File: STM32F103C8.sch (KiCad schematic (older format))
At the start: 0 parts

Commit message: STM32F103C8
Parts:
- added U?: STM32F103C8Tx, Package_QFP:LQFP-48_7x7mm_P0.5mm, symbol MCU_ST_STM32F1:STM32F103C8Tx
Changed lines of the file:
@@
 $Descr A4 11693 8268
 encoding utf-8
-Sheet 1 1
+Sheet 5 5
 Title ""
 Date ""
@@
 Comment4 ""
 $EndDescr
+$Comp
+L MCU_ST_STM32F1:STM32F103C8Tx U?
+U 1 1 5CEC658E
+P 5600 3900
+F 0 "U?" H 5550 2311 50  0000 C CNN
+F 1 "STM32F103C8Tx" H 5550 2220 50  0000 C CNN
+F 2 "Package_QFP:LQFP-48_7x7mm_P0.5mm" H 5000 2500 50  0001 R CNN
+F 3 "http://www.st.com/st-web-ui/static/active/en/resource/technical/document/datasheet/CD00161566.pdf" H 5600 3900 50  0001 C CNN
+	1    5600 3900
+	1    0    0    -1
+$EndComp
 $EndSCHEMATC

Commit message: USB - Boot sel - Serial - STM32
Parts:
- added C? (x2): 20p, Capacitor_SMD:C_0805_2012Metric_Pad1.15x1.40mm_HandSolder, symbol Device:C
- added C? (x4): 100n, Capacitor_SMD:C_0805_2012Metric_Pad1.15x1.40mm_HandSolder, symbol Device:C
- added D?: LED, LED_SMD:LED_0805_2012Metric_Pad1.15x1.40mm_HandSolder, symbol Device:LED
- added J?: UART, Connector_PinHeader_2.54mm:PinHeader_1x04_P2.54mm_Vertical, symbol Connector_Generic:Conn_01x04
- added J?: BOOT, Connector_PinHeader_2.54mm:PinHeader_2x03_P2.54mm_Vertical, symbol Connector_Generic:Conn_02x03_Odd_Even
- added J?: USB_B_Micro, symbol Connector:USB_B_Micro
- added R?: 1k, Resistor_SMD:R_0805_2012Metric_Pad1.15x1.40mm_HandSolder, symbol Device:R
- added R?: 0R, Resistor_SMD:R_0805_2012Metric_Pad1.15x1.40mm_HandSolder, symbol Device:R
- added R?: 0R, Jumper:SolderJumper-2_P1.3mm_Bridged_RoundedPad1.0x1.5mm, symbol Device:R
- added R? (x2): 100k, Resistor_SMD:R_0805_2012Metric_Pad1.15x1.40mm_HandSolder, symbol Device:R
- added R? (x2): 10k, Resistor_SMD:R_0805_2012Metric_Pad1.15x1.40mm_HandSolder, symbol Device:R
- added R?: 1k5, Resistor_SMD:R_0805_2012Metric_Pad1.15x1.40mm_HandSolder, symbol Device:R
- added R?: 10R, Resistor_SMD:R_0805_2012Metric_Pad1.15x1.40mm_HandSolder, symbol Device:R
- added U?: AMS1117-3.3, Package_TO_SOT_SMD:SOT-223-3_TabPin2, symbol Regulator_Linear:AMS1117-3.3
- added Y?: 8 MHz, Crystal:Crystal_HC49-U_Vertical, symbol Device:Crystal
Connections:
- net STM32_PA0: now reaches U?.10 (PA0)
- net STM32_PA1: now reaches U?.11 (PA1)
- net STM32_PA2: now reaches U?.12 (PA2)
- net STM32_PA3: now reaches U?.13 (PA3)
- net STM32_PA4: now reaches U?.14 (PA4)
- net STM32_PA5: now reaches U?.15 (PA5)
- net STM32_PA6: now reaches U?.16 (PA6)
- net STM32_PA7: now reaches U?.17 (PA7)
- net STM32_PB0: now reaches U?.18 (PB0)
- net STM32_PB1: now reaches U?.19 (PB1)
- net STM32_PC13: now reaches U?.2 (PC13)
- net STM32_PB2: now reaches U?.20 (PB2)
- net STM32_PB2: now also R?.2
- net STM32_PB10: now reaches U?.21 (PB10)
- net STM32_PB11: now reaches U?.22 (PB11)
- net GND: now reaches U?.23 (VSS)
- net GND: now also U?.35 (VSS), U?.47 (VSS), C?.1, C?.1, C?.1, C?.2, C?.2, D?.1 (K), J?.1 (Pin_1), J?.2 (Pin_2), J?.4 (Pin_4), J?.5 (GND), J?.6 (Shield), R?.2, U?.1 (GND)
- net +3V3: now reaches U?.24 (VDD)
- net +3V3: now also U?.36 (VDD), U?.48 (VDD), C?.2, C?.2, C?.2, J?.1 (Pin_1), J?.5 (Pin_5), J?.6 (Pin_6), R?.1, R?.2, R?.2, R?.2, U?.2 (VO)
- net STM32_PB12: now reaches U?.25 (PB12)
- net STM32_PB13: now reaches U?.26 (PB13)
- net STM32_PB14: now reaches U?.27 (PB14)
- net STM32_PB15: now reaches U?.28 (PB15)
- net STM32_PA8: now reaches U?.29 (PA8)
- net STM32_PC14: now reaches U?.3 (PC14)
- net STM32_PA9: now reaches U?.30 (PA9)
- net STM32_PA10: now reaches U?.31 (PA10)
- net STM32_PA11: now reaches U?.32 (PA11)
- net STM32_PA11: now also J?.2 (D-)
- net STM32_PA12: now reaches U?.33 (PA12)
- net STM32_PA12: now also J?.3 (D+), R?.2
- net STM32_PA13: now reaches U?.34 (PA13)
- net STM32_PA13: now also J?.2 (Pin_2), R?.1
- net STM32_PA14: now reaches U?.37 (PA14)
- net STM32_PA14: now also J?.3 (Pin_3), R?.1
- net STM32_PA15: now reaches U?.38 (PA15)
- net STM32_PB3: now reaches U?.39 (PB3)
- net STM32_PC15: now reaches U?.4 (PC15)
- net STM32_PB4: now reaches U?.40 (PB4)
- net STM32_PB5: now reaches U?.41 (PB5)
- net STM32_PB6: now reaches U?.42 (PB6)
- net STM32_PB7: now reaches U?.43 (PB7)
- net STM32_Boot0: now reaches U?.44 (BOOT0)
- net STM32_Boot0: now also R?.2
- net STM32_PB8: now reaches U?.45 (PB8)
- net STM32_PB9: now reaches U?.46 (PB9)
- net at U?.5 (PD0): now also C?.1, Y?.1
- net at U?.6 (PD1): now also C?.1, Y?.2
- net STM32_reset: now reaches U?.7 (NRST)
- net GNDA: now reaches U?.8 (VSSA)
- net GNDA: now also C?.1, R?.1
- net +3.3VA: now reaches U?.9 (VDDA)
- net +3.3VA: now also C?.2, R?.1
- new net: D?.2 (A), R?.1
- new net: J?.3 (Pin_3), R?.1
- new net: J?.4 (Pin_4), R?.1
- new net: J?.1 (VBUS), R?.1
- new net +5V: R?.2, U?.3 (VI)
- new net 0_LED: R?.2
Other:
- note added: "Annotation according to \nhttps://github.com/MCUdude/MightyCore"

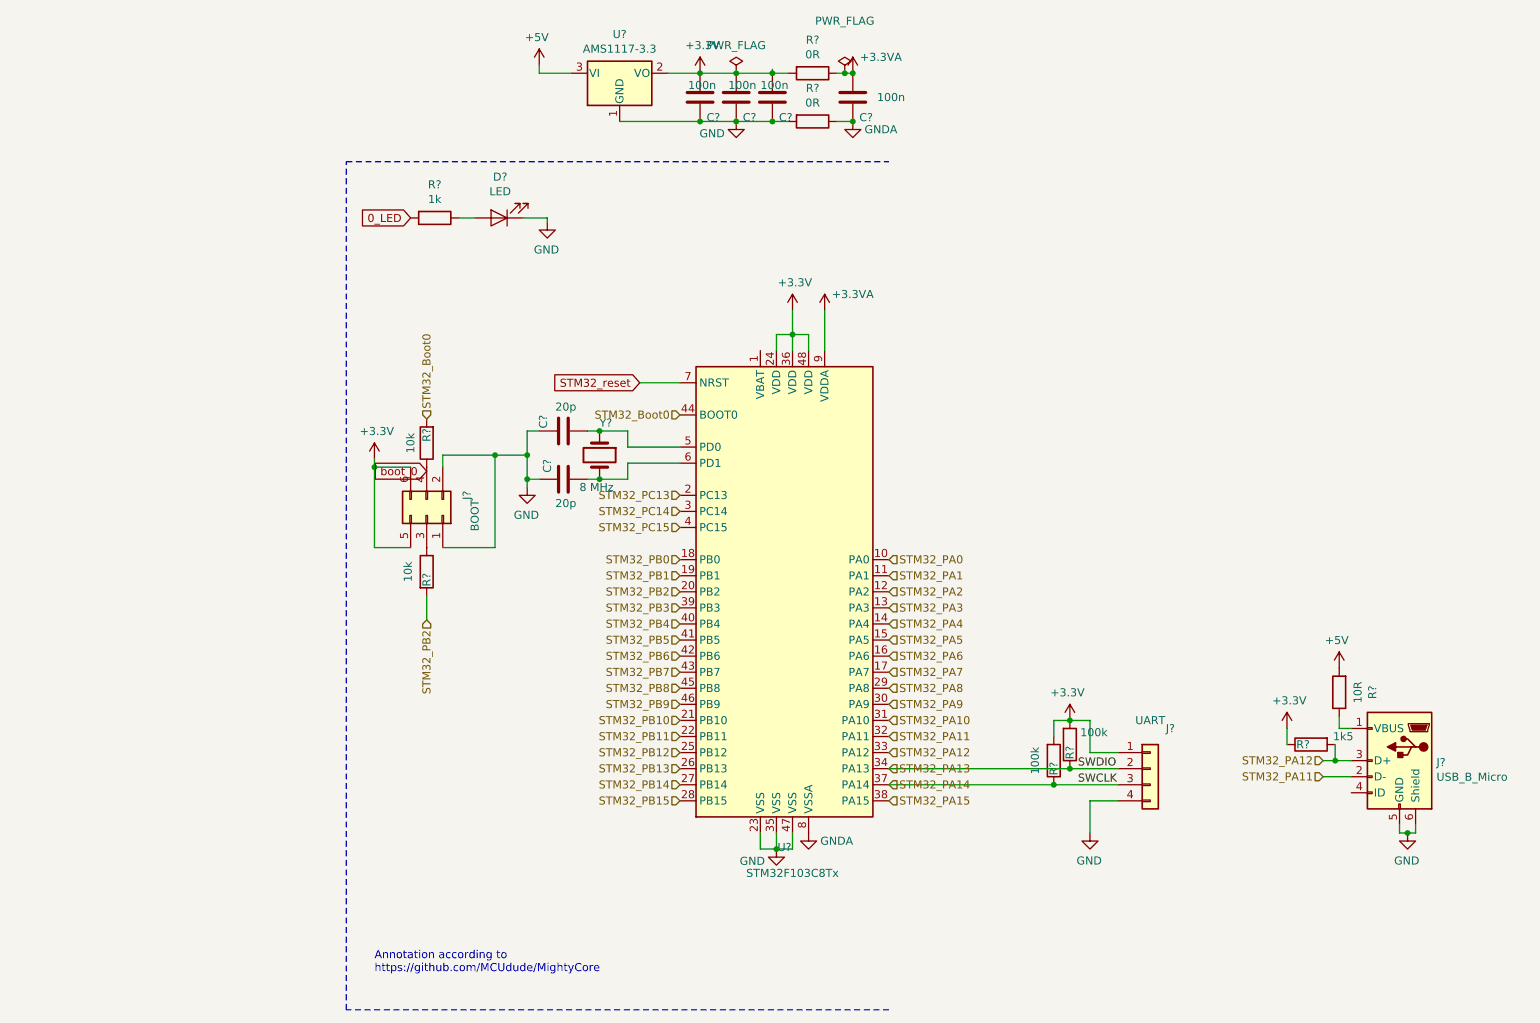
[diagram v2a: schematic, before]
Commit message: STM32 DAC and Analog input
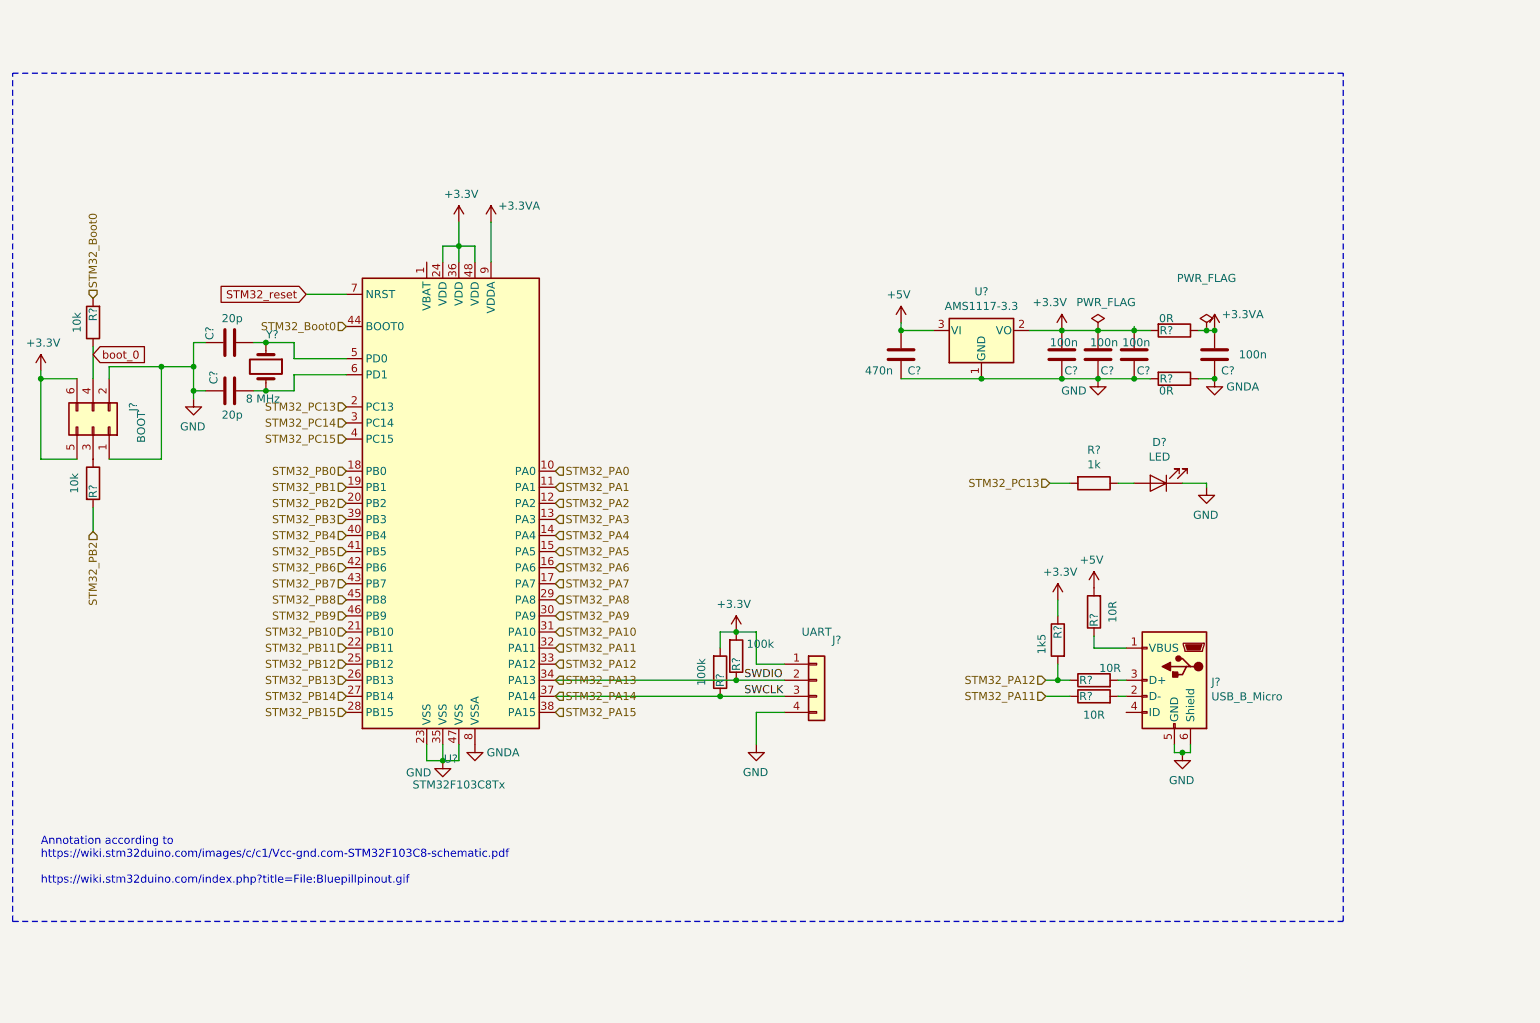
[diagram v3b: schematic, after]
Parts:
- added C?: 470n, Capacitor_SMD:C_0805_2012Metric_Pad1.15x1.40mm_HandSolder, symbol Device:C
- added R? (x2): 10R, Resistor_SMD:R_0805_2012Metric_Pad1.15x1.40mm_HandSolder, symbol Device:R
- J?: footprint (none) -> Connector_USB:USB_Micro-B_Wuerth_629105150521
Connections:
- net 0_LED is gone; now on net STM32_PC13: R?.2
- net +5V: now also C?.2
- net GND: now also C?.1
- net STM32_PA11: now also R?.1; no longer J?.2 (D-)
- net STM32_PA12: now also R?.1; no longer J?.3 (D+)
- net boot_0: now also J?.4 (Pin_4), R?.1
- new net: J?.2 (D-), R?.2
- new net: J?.3 (D+), R?.2
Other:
- note added: "Annotation according to \nhttps://wiki.stm32duino.com/images/c/c1/Vcc-gnd.com-STM32F103C8-schematic.pdf\n\nhttps://wiki.stm32duino.com/index.php?title=File:Bluepillpinout.gif\n"
- note removed: "Annotation according to \nhttps://github.com/MCUdude/MightyCore"
- moved on the sheet: C?, D?, J?, R?, U?, Y?

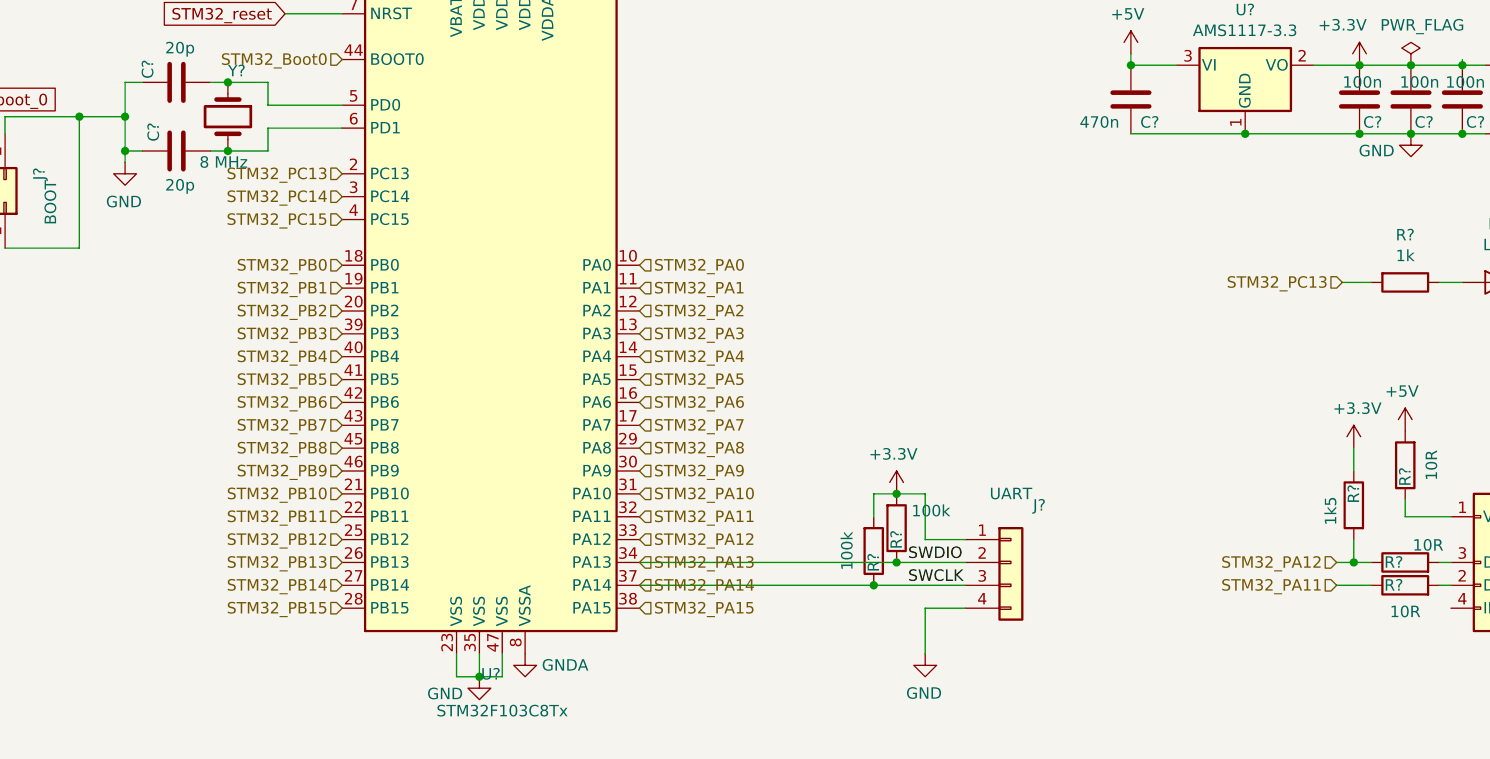
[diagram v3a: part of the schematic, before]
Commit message: STM32 Pin names for serial and USB
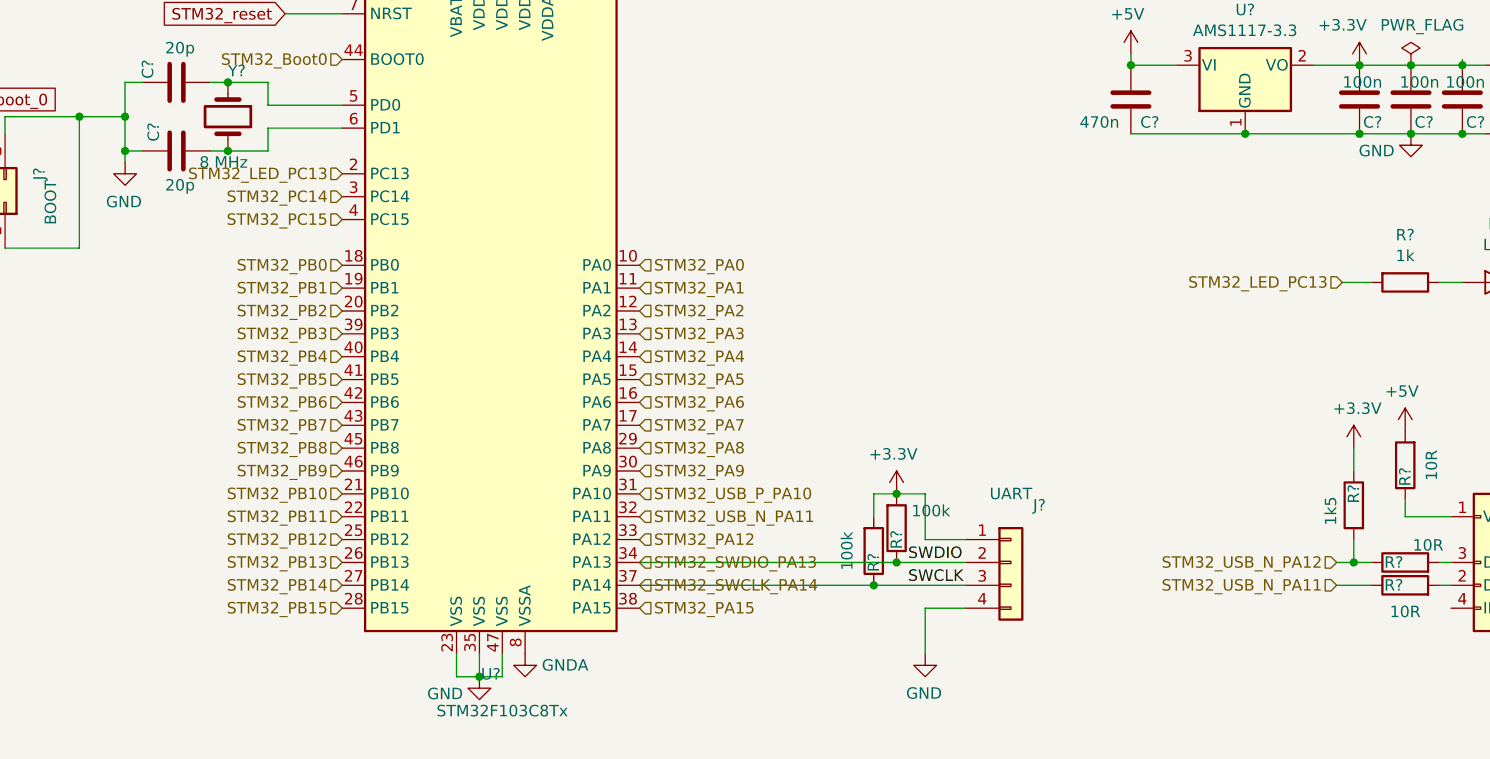
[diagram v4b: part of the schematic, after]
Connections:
- net STM32_PA12: no longer R?.1, R?.2
- net STM32_PA10 renamed STM32_USB_P_PA10
- net STM32_PA11 renamed STM32_USB_N_PA11
- net STM32_PA13 renamed STM32_SWDIO_PA13
- net STM32_PA14 renamed STM32_SWCLK_PA14
- net STM32_PC13 renamed STM32_LED_PC13
- new net STM32_USB_N_PA12: R?.1, R?.2
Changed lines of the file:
@@
 STM32_PA9
 Text HLabel 4125 4150 2    50   Input ~ 0
-STM32_PA10
+STM32_USB_P_PA10
 Text HLabel 4125 4250 2    50   Input ~ 0
-STM32_PA11
+STM32_USB_N_PA11
 Text HLabel 4125 4350 2    50   Input ~ 0
 STM32_PA12
 Text HLabel 4125 4450 2    50   Input ~ 0
-STM32_PA13
+STM32_SWDIO_PA13
 Text HLabel 4125 4550 2    50   Input ~ 0
-STM32_PA14
+STM32_SWCLK_PA14
 Text HLabel 4125 4650 2    50   Input ~ 0
 STM32_PA15
 Text HLabel 2825 2750 0    50   Input ~ 0
-STM32_PC13
+STM32_LED_PC13
 Text HLabel 2825 2850 0    50   Input ~ 0
 STM32_PC14
@@
 $EndComp
 Text HLabel 7175 4550 0    50   Input ~ 0
-STM32_PA11
+STM32_USB_N_PA11
 Text HLabel 7175 4450 0    50   Input ~ 0
-STM32_PA12
+STM32_USB_N_PA12
 Wire Wire Line
 	7175 4450 7250 4450
@@
 	7625 4450 7675 4450
 Text HLabel 7200 3225 0    50   Input ~ 0
-STM32_PC13
+STM32_LED_PC13
 Wire Wire Line
 	7200 3225 7325 3225
